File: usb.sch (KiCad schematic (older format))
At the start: 2 parts, among them U9 NX5P3090UKZ

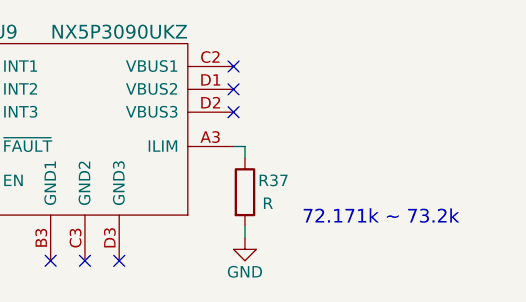
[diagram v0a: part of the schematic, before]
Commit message: Figure out 5.0V buck-boost's inductor value, include inductor current calculations
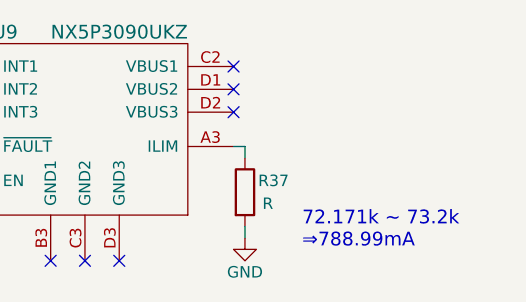
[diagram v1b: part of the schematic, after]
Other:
- note added: "72.171k ~~ 73.2k\n⇒788.99mA"
- note removed: "72.171k ~~ 73.2k"

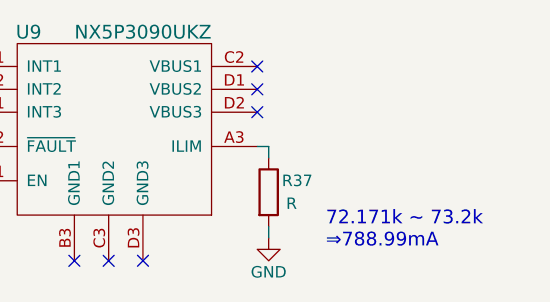
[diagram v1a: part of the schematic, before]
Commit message: Use MIC2876 instead of RT6150A due to several advantages which are noted in the schematic
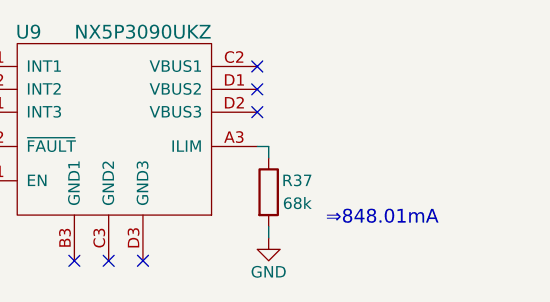
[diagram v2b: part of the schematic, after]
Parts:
- R37: value R -> 68k
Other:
- note added: "⇒848.01mA"
- note removed: "72.171k ~~ 73.2k\n⇒788.99mA"
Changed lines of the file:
@@
 P 5950 3750
 F 0 "R37" H 6075 3800 50  0000 C CNN
-F 1 "R" H 6050 3700 50  0000 C CNN
+F 1 "68k" H 6075 3700 50  0000 C CNN
 F 2 "" V 5880 3750 50  0001 C CNN
 F 3 "" H 5950 3750 50  0001 C CNN
@@
 NoConn ~ 5900 3300
 NoConn ~ 5900 3400
-Text Notes 6200 4000 0    60   ~ 0
-72.171k ~~ 73.2k\n⇒788.99mA
 NoConn ~ 5250 4050
 NoConn ~ 5400 4050
@@
 EndData
 $EndBitmap
+Text Notes 6200 3900 0    60   ~ 0
+⇒848.01mA
 $EndSCHEMATC

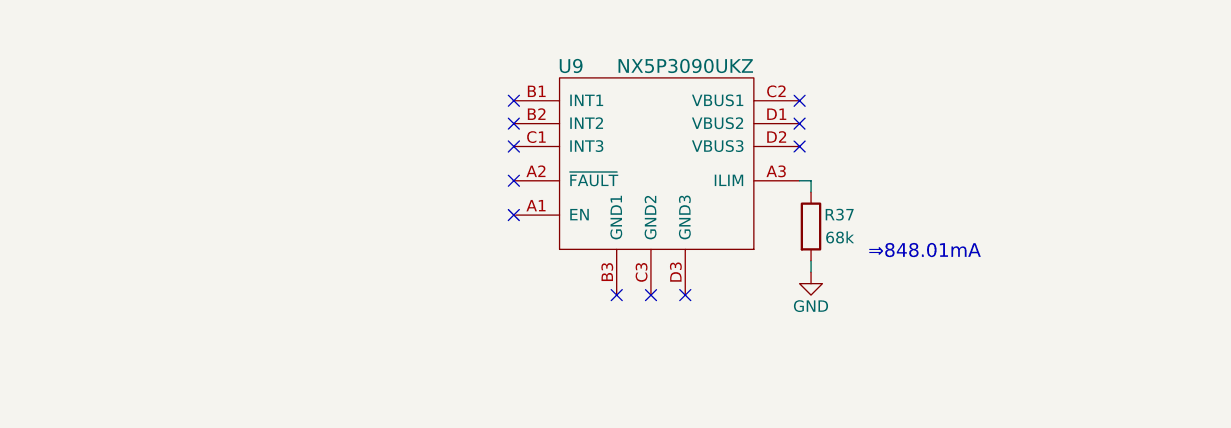
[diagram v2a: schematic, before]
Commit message: Use a buck for the 1.8V rail for efficiency, include power line ferrite bead, change main buck-boost output caps to 0805 ones, move the main regulator's input caps to the VIN node, include USB power switch circuit's components
The 1.8V buck has a drop-in: "ST1S12G18R"
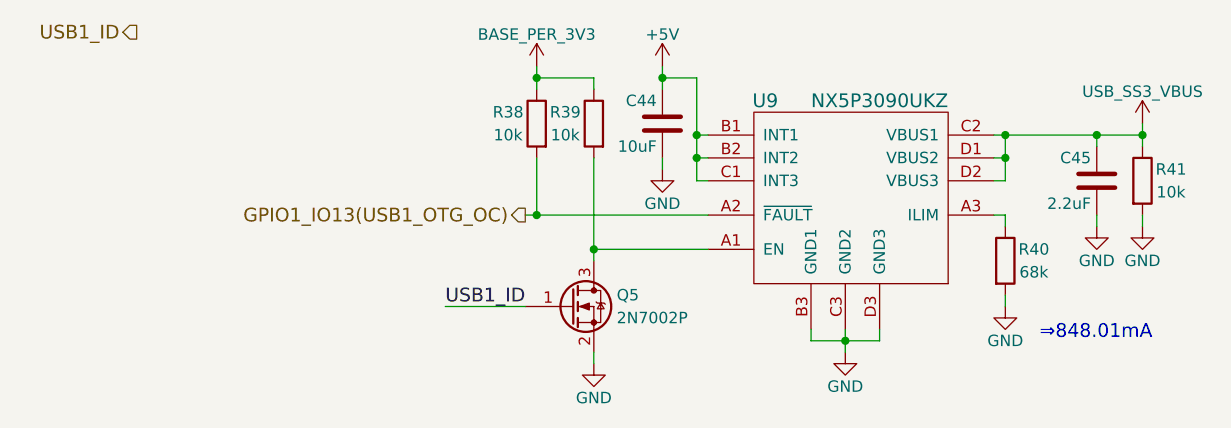
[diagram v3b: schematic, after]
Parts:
- added C44: 10uF, symbol C
- added C45: 2.2uF, symbol C
- added Q5: 2N7002P, symbol Q_NMOS_GSD
- added R38, R39, R41: 10k, symbol R
- renumbered R37 to R40
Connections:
- net GND: now also U9.B3 (GND1), U9.C3 (GND2), U9.D3 (GND3), C44.2, C45.2, Q5.2 (S), R41.2
- net at U9.A1 (EN): now also Q5.3 (D), R39.2
- net GPIO1_IO13(USB1_OTG_OC): now reaches U9.A2 (~FAULT)
- net GPIO1_IO13(USB1_OTG_OC): now also R38.2
- net +5V: now reaches U9.B1 (INT1)
- net +5V: now also U9.B2 (INT2), U9.C1 (INT3), C44.1
- net USB_SS3_VBUS: now reaches U9.C2 (VBUS1)
- net USB_SS3_VBUS: now also U9.D1 (VBUS2), U9.D2 (VBUS3), C45.1, R41.1
- new net BASE_PER_3V3: R38.1, R39.1
- new net USB1_ID: Q5.1 (G)
- no-connect marks 11 -> 0
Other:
- moved on the sheet: R40, U9

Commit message: Include UART debug interface/header, using a 74LVC2G241 buffer which is 5V tolerant so that either 3.3V or 5V UART cables could be used
Six pin header used so that either 6-pin fixed, 4-pin, or 3-pin cables can be used. Only RX, TX, and GND are used since Vcc, RTS#, and CTS# is unneeded, the other three pins are NC.
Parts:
- renumbered C44 to C47, C45 to C48
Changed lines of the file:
@@
 $Descr A4 11693 8268
 encoding utf-8
-Sheet 7 8
+Sheet 7 9
 Title ""
 Date "2018-04-05"
@@
 $EndComp
 $Comp
-L GND #PWR088
+L GND #PWR089
 U 1 1 5ACF654F
 P 6800 4100
-F 0 "#PWR088" H 6800 3850 50  0001 C CNN
+F 0 "#PWR089" H 6800 3850 50  0001 C CNN
 F 1 "GND" H 6800 3950 50  0000 C CNN
 F 2 "" H 6800 4100 50  0001 C CNN
@@
 $EndComp
 $Comp
-L C C44
+L C C47
 U 1 1 5ACBFFF9
 P 5300 3300
-F 0 "C44" H 5325 3400 50  0000 L CNN
+F 0 "C47" H 5325 3400 50  0000 L CNN
 F 1 "10uF" H 5325 3200 50  0000 L CNN
 F 2 "" H 5338 3150 50  0001 C CNN
@@
 $EndComp
 $Comp
-L C C45
+L C C48
 U 1 1 5ACC0253
 P 7200 3550
-F 0 "C45" H 7225 3650 50  0000 L CNN
+F 0 "C48" H 7225 3650 50  0000 L CNN
 F 1 "2.2uF" H 7225 3450 50  0000 L CNN
 F 2 "" H 7238 3400 50  0001 C CNN
@@
 $EndComp
 $Comp
-L GND #PWR089
+L GND #PWR090
 U 1 1 5ACC064A
 P 5300 3500
-F 0 "#PWR089" H 5300 3250 50  0001 C CNN
+F 0 "#PWR090" H 5300 3250 50  0001 C CNN
 F 1 "GND" H 5300 3350 50  0000 C CNN
 F 2 "" H 5300 3500 50  0001 C CNN
@@
 Connection ~ 5450 3350
 $Comp
-L +5V #PWR090
+L +5V #PWR091
 U 1 1 5ACC0801
 P 5300 3050
-F 0 "#PWR090" H 5300 2900 50  0001 C CNN
+F 0 "#PWR091" H 5300 2900 50  0001 C CNN
 F 1 "+5V" H 5300 3190 50  0000 C CNN
 F 2 "" H 5300 3050 50  0001 C CNN
@@
 GPIO1_IO13(USB1_OTG_OC)
 $Comp
-L BASE_PER_3V3 #PWR091
+L BASE_PER_3V3 #PWR092
 U 1 1 5ACC0CDC
 P 4750 3050
-F 0 "#PWR091" H 4750 2900 50  0001 C CNN
+F 0 "#PWR092" H 4750 2900 50  0001 C CNN
 F 1 "BASE_PER_3V3" H 4750 3190 50  0000 C CNN
 F 2 "" H 4750 3050 50  0001 C CNN
@@
 	4350 4100 4700 4100
 $Comp
-L GND #PWR092
+L GND #PWR093
 U 1 1 5ACC18BD
 P 5000 4350
-F 0 "#PWR092" H 5000 4100 50  0001 C CNN
+F 0 "#PWR093" H 5000 4100 50  0001 C CNN
 F 1 "GND" H 5000 4200 50  0000 C CNN
 F 2 "" H 5000 4350 50  0001 C CNN
@@
 	5000 4350 5000 4300
 $Comp
-L GND #PWR093
+L GND #PWR094
 U 1 1 5ACC1A19
 P 6100 4300
-F 0 "#PWR093" H 6100 4050 50  0001 C CNN
+F 0 "#PWR094" H 6100 4050 50  0001 C CNN
 F 1 "GND" H 6100 4150 50  0000 C CNN
 F 2 "" H 6100 4300 50  0001 C CNN
@@
 Connection ~ 6100 4250
 $Comp
-L GND #PWR094
+L GND #PWR095
 U 1 1 5ACC1F9D
 P 7200 3750
-F 0 "#PWR094" H 7200 3500 50  0001 C CNN
+F 0 "#PWR095" H 7200 3500 50  0001 C CNN
 F 1 "GND" H 7200 3600 50  0000 C CNN
 F 2 "" H 7200 3750 50  0001 C CNN
@@
 Connection ~ 7400 3350
 $Comp
-L GND #PWR095
+L GND #PWR096
 U 1 1 5ACC294F
 P 7400 3750
-F 0 "#PWR095" H 7400 3500 50  0001 C CNN
+F 0 "#PWR096" H 7400 3500 50  0001 C CNN
 F 1 "GND" H 7400 3600 50  0000 C CNN
 F 2 "" H 7400 3750 50  0001 C CNN
@@
 	7400 3700 7400 3750
 $Comp
-L USB_SS3_VBUS #PWR096
+L USB_SS3_VBUS #PWR097
 U 1 1 5ACC617E
 P 7400 3300
-F 0 "#PWR096" H 7400 3150 50  0001 C CNN
+F 0 "#PWR097" H 7400 3150 50  0001 C CNN
 F 1 "USB_SS3_VBUS" H 7400 3440 50  0000 C CNN
 F 2 "" H 7400 3300 50  0001 C CNN
